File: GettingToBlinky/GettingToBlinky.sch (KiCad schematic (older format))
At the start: 7 parts

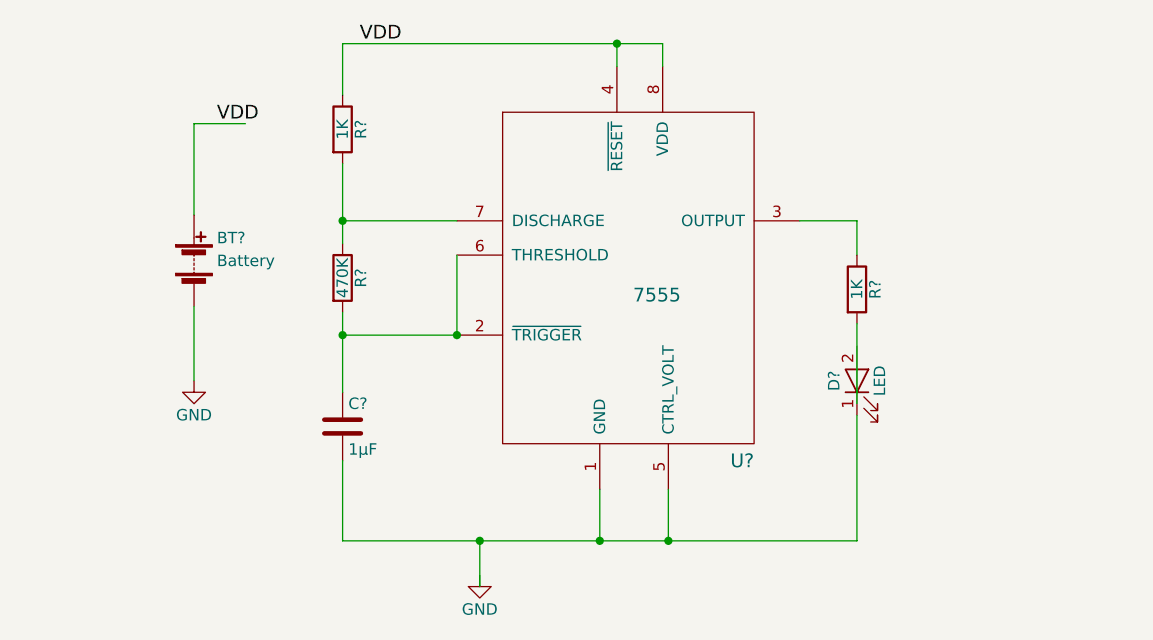
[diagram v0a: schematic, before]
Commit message: created net list
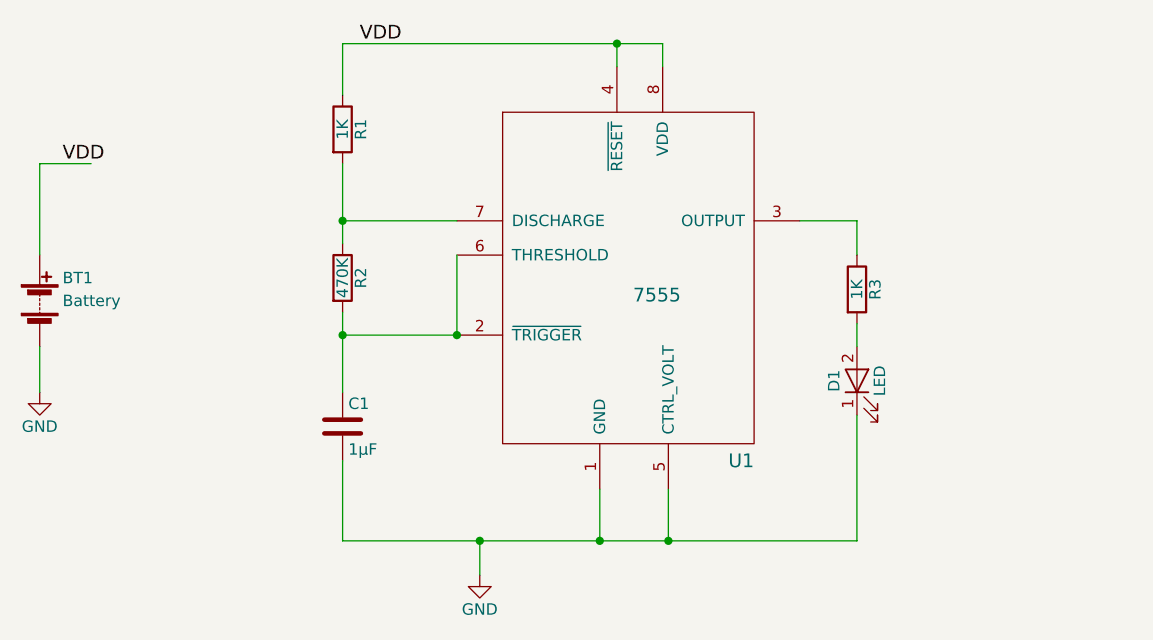
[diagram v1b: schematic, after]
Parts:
- gave numbers to parts that had none: 7
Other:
- moved on the sheet: BT1
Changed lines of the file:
@@
 $EndDescr
 $Comp
-L 7555 U?
+L 7555 U1
 U 1 1 58DA3579
 P 5300 3800
-F 0 "U?" H 5850 3000 60  0000 R CNN
+F 0 "U1" H 5850 3000 60  0000 R CNN
 F 1 "7555" H 5425 3725 60  0000 C CNN
 F 2 "" H 4875 4375 60  0001 C CNN
@@
 $EndComp
 $Comp
-L R R?
+L R R1
 U 1 1 58DA3631
 P 4050 3150
-F 0 "R?" V 4130 3150 50  0000 C CNN
+F 0 "R1" V 4130 3150 50  0000 C CNN
 F 1 "1K" V 4050 3150 50  0000 C CNN
 F 2 "" V 3980 3150 50  0001 C CNN
@@
 $EndComp
 $Comp
-L R R?
+L R R2
 U 1 1 58DA36C3
 P 4050 3800
-F 0 "R?" V 4130 3800 50  0000 C CNN
+F 0 "R2" V 4130 3800 50  0000 C CNN
 F 1 "470K" V 4050 3800 50  0000 C CNN
 F 2 "" V 3980 3800 50  0001 C CNN
@@
 $EndComp
 $Comp
-L R R?
+L R R3
 U 1 1 58DA36F0
 P 6300 3850
-F 0 "R?" V 6380 3850 50  0000 C CNN
+F 0 "R3" V 6380 3850 50  0000 C CNN
 F 1 "1K" V 6300 3850 50  0000 C CNN
 F 2 "" V 6230 3850 50  0001 C CNN
@@
 $EndComp
 $Comp
-L C C?
+L C C1
 U 1 1 58DA3730
 P 4050 4450
-F 0 "C?" H 4075 4550 50  0000 L CNN
+F 0 "C1" H 4075 4550 50  0000 L CNN
 F 1 "1µF" H 4075 4350 50  0000 L CNN
 F 2 "" H 4088 4300 50  0001 C CNN
@@
 $EndComp
 $Comp
-L LED D?
+L LED D1
 U 1 1 58DA3776
 P 6300 4250
-F 0 "D?" H 6300 4350 50  0000 C CNN
+F 0 "D1" H 6300 4350 50  0000 C CNN
 F 1 "LED" H 6300 4150 50  0000 C CNN
 F 2 "" H 6300 4250 50  0001 C CNN
@@
 	6300 3550 6300 3700
 Wire Wire Line
-	6300 4000 6300 4350
+	6300 4000 6300 4100
 Connection ~ 4550 4050
 Wire Wire Line
@@
 VDD
 $Comp
-L GND #PWR?
+L GND #PWR01
 U 1 1 58DA3C39
 P 4650 5100
-F 0 "#PWR?" H 4650 4850 50  0001 C CNN
+F 0 "#PWR01" H 4650 4850 50  0001 C CNN
 F 1 "GND" H 4650 4950 50  0000 C CNN
 F 2 "" H 4650 5100 50  0001 C CNN
@@
 	1    0    0    -1
 $EndComp
-Wire Wire Line
-	4650 4950 4650 5150
-Connection ~ 4650 4950
 $Comp
-L Battery BT?
+L Battery BT1
 U 1 1 58DA3EDF
-P 3400 3725
-F 0 "BT?" H 3500 3825 50  0000 L CNN
-F 1 "Battery" H 3500 3725 50  0000 L CNN
-F 2 "" V 3400 3785 50  0001 C CNN
-F 3 "" V 3400 3785 50  0001 C CNN
-	1    3400 3725
+P 2725 3900
+F 0 "BT1" H 2825 4000 50  0000 L CNN
+F 1 "Battery" H 2825 3900 50  0000 L CNN
+F 2 "" V 2725 3960 50  0001 C CNN
+F 3 "" V 2725 3960 50  0001 C CNN
+	1    2725 3900
 	1    0    0    -1
 $EndComp
 Wire Wire Line
-	3400 3525 3400 3125
-Wire Wire Line
-	3400 3125 3625 3125
-Wire Wire Line
-	3400 3925 3400 4250
-Text Label 3500 3125 0    60   ~ 0
+	2725 3300 2950 3300
+Text Label 2825 3300 0    60   ~ 0
 VDD
 $Comp
-L GND #PWR?
+L GND #PWR02
 U 1 1 58DA3FAB
-P 3400 4250
-F 0 "#PWR?" H 3400 4000 50  0001 C CNN
-F 1 "GND" H 3400 4100 50  0000 C CNN
-F 2 "" H 3400 4250 50  0001 C CNN
-F 3 "" H 3400 4250 50  0001 C CNN
-	1    3400 4250
+P 2725 4300
+F 0 "#PWR02" H 2725 4050 50  0001 C CNN
+F 1 "GND" H 2725 4150 50  0000 C CNN
+F 2 "" H 2725 4300 50  0001 C CNN
+F 3 "" H 2725 4300 50  0001 C CNN
+	1    2725 4300
 	1    0    0    -1
 $EndComp
+Wire Wire Line
+	2725 3300 2725 3700
+Connection ~ 4650 4950
+Wire Wire Line
+	4650 4950 4650 5100
+Wire Wire Line
+	2725 4100 2725 4300
 $EndSCHEMATC

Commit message: created correct net list
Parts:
- C1: footprint (none) -> Capacitors_SMD:C_1206_HandSoldering
- D1: footprint (none) -> LEDs:LED-3MM
- R1, R2, R3: footprint (none) -> Resistors_SMD:R_0805_HandSoldering
- U1: footprint (none) -> Housings_SOIC:SOIC-8_3.9x4.9mm_Pitch1.27mm
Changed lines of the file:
@@
 LIBS:valves
 LIBS:GTB
+LIBS:GettingToBlinky-cache
 EELAYER 25 0
 EELAYER END
@@
 F 0 "U1" H 5850 3000 60  0000 R CNN
 F 1 "7555" H 5425 3725 60  0000 C CNN
-F 2 "" H 4875 4375 60  0001 C CNN
+F 2 "Housings_SOIC:SOIC-8_3.9x4.9mm_Pitch1.27mm" H 4875 4375 60  0001 C CNN
 F 3 "" H 4875 4375 60  0001 C CNN
 	1    5300 3800
@@
 F 0 "R1" V 4130 3150 50  0000 C CNN
 F 1 "1K" V 4050 3150 50  0000 C CNN
-F 2 "" V 3980 3150 50  0001 C CNN
+F 2 "Resistors_SMD:R_0805_HandSoldering" V 3980 3150 50  0001 C CNN
 F 3 "" H 4050 3150 50  0001 C CNN
 	1    4050 3150
@@
 F 0 "R2" V 4130 3800 50  0000 C CNN
 F 1 "470K" V 4050 3800 50  0000 C CNN
-F 2 "" V 3980 3800 50  0001 C CNN
+F 2 "Resistors_SMD:R_0805_HandSoldering" V 3980 3800 50  0001 C CNN
 F 3 "" H 4050 3800 50  0001 C CNN
 	1    4050 3800
@@
 F 0 "R3" V 6380 3850 50  0000 C CNN
 F 1 "1K" V 6300 3850 50  0000 C CNN
-F 2 "" V 6230 3850 50  0001 C CNN
+F 2 "Resistors_SMD:R_0805_HandSoldering" V 6230 3850 50  0001 C CNN
 F 3 "" H 6300 3850 50  0001 C CNN
 	1    6300 3850
@@
 F 0 "C1" H 4075 4550 50  0000 L CNN
 F 1 "1µF" H 4075 4350 50  0000 L CNN
-F 2 "" H 4088 4300 50  0001 C CNN
+F 2 "Capacitors_SMD:C_1206_HandSoldering" H 4088 4300 50  0001 C CNN
 F 3 "" H 4050 4450 50  0001 C CNN
 	1    4050 4450
@@
 F 0 "D1" H 6300 4350 50  0000 C CNN
 F 1 "LED" H 6300 4150 50  0000 C CNN
-F 2 "" H 6300 4250 50  0001 C CNN
+F 2 "LEDs:LED-3MM" H 6300 4250 50  0001 C CNN
 F 3 "" H 6300 4250 50  0001 C CNN
 	1    6300 4250

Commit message: finished pcb layout
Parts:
- BT1: footprint (none) -> GTB:BatteryHolder
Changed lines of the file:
@@
 F 0 "BT1" H 2825 4000 50  0000 L CNN
 F 1 "Battery" H 2825 3900 50  0000 L CNN
-F 2 "" V 2725 3960 50  0001 C CNN
+F 2 "GTB:BatteryHolder" V 2725 3960 50  0001 C CNN
 F 3 "" V 2725 3960 50  0001 C CNN
 	1    2725 3900

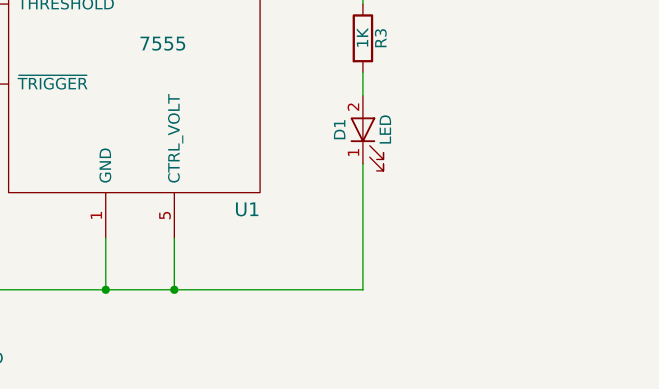
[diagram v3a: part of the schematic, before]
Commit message: removed pin5 connection, re-generated pcb
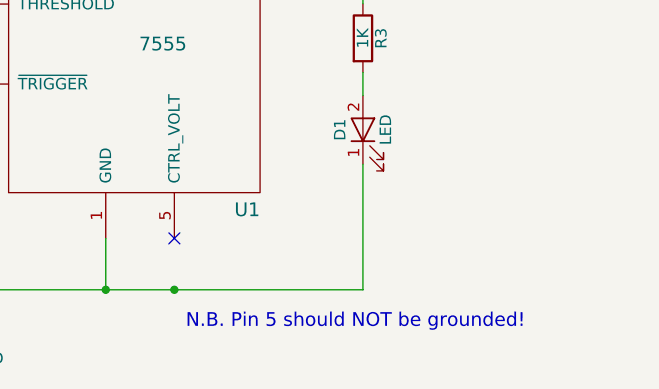
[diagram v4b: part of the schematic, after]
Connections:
- wire segments 21 -> 20
- no-connect marks 0 -> 1
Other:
- note added: "N.B. Pin 5 should NOT be grounded!"
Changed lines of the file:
@@
 Wire Wire Line
 	5175 4950 5175 4725
-Wire Wire Line
-	5475 4950 5475 4725
 Connection ~ 5175 4950
 Wire Wire Line
 	6300 4950 6300 4400
-Connection ~ 5475 4950
 Wire Wire Line
 	5250 2875 5250 2775
@@
 Wire Wire Line
 	2725 4100 2725 4300
+Text Notes 5525 5125 0    60   ~ 0
+N.B. Pin 5 should NOT be grounded!
+NoConn ~ 5475 4725
+Connection ~ 5475 4950
 $EndSCHEMATC
